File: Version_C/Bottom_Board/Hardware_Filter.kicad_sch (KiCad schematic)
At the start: 37 parts, among them U1 LM324, U2 LM324

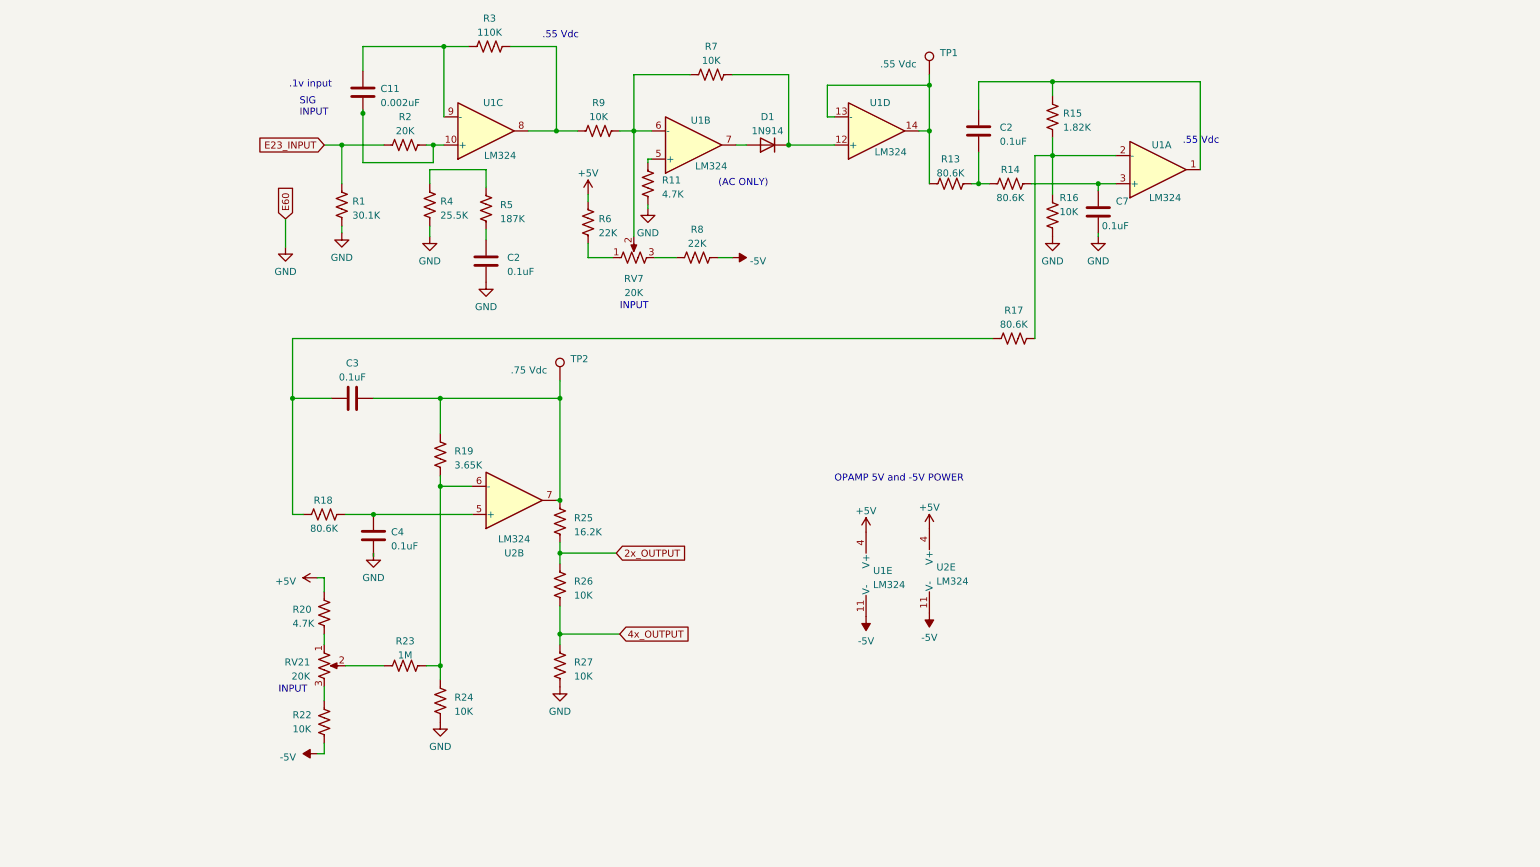
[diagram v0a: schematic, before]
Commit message: fixed directory overwrite
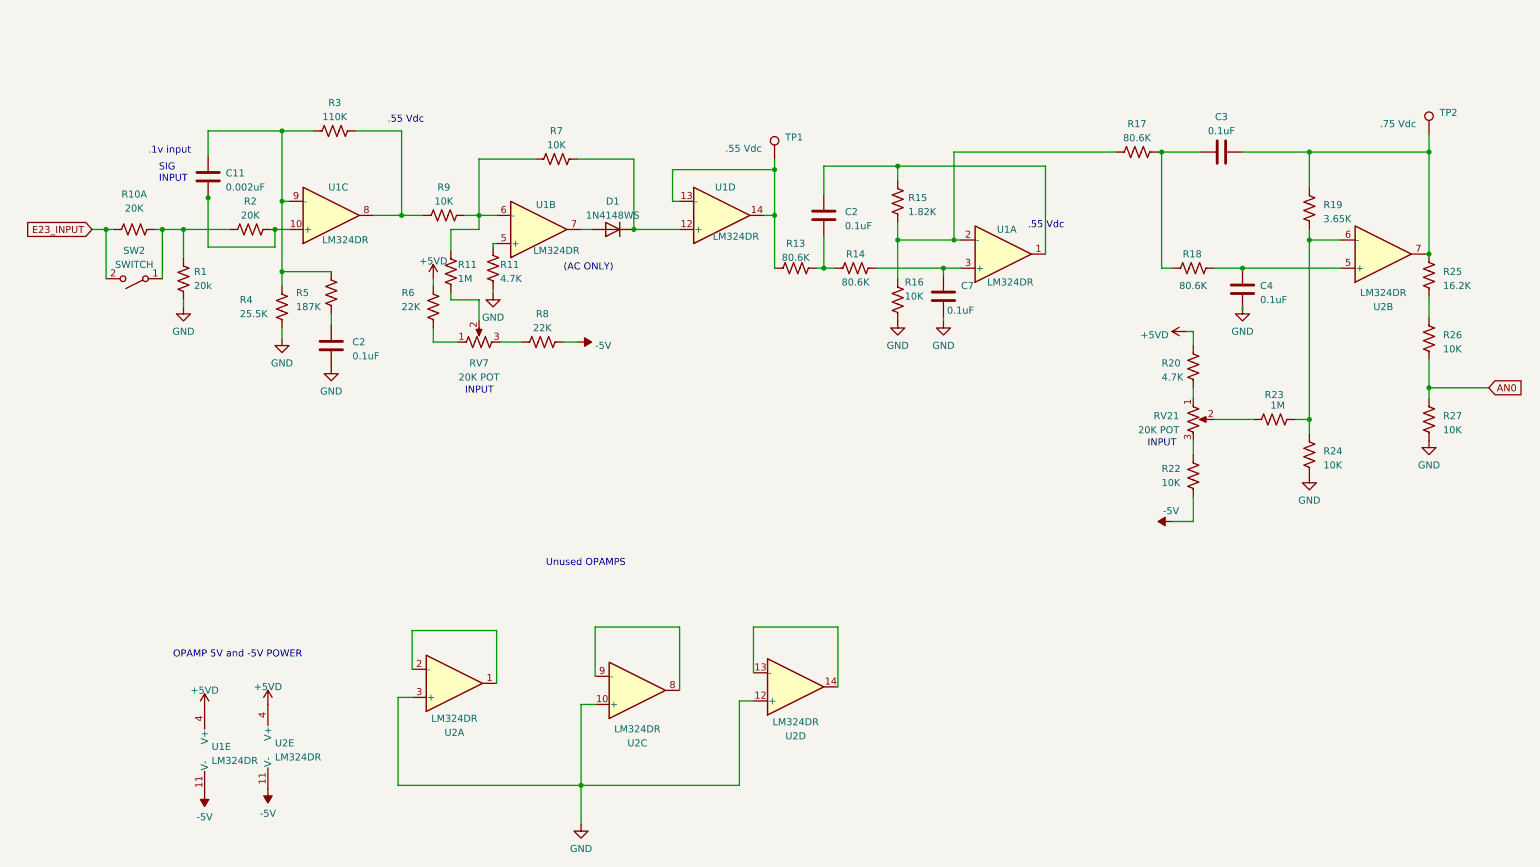
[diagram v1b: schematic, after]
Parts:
- added R10A: 20K, Resistor_SMD:R_0603_1608Metric, symbol Device:R_US
- added R11: 1M, Resistor_SMD:R_0603_1608Metric, symbol Device:R_US
- added SW2: SWITCH, symbol Switch:SW_SPST
- added unit 1 of U2
- added unit 4 of U2
- added unit 3 of U2
- D1: value 1N914 -> 1N4148WS; footprint Diode_SMD:D_0603_1608Metric -> bot_lib:Diode_1N4148WS
- R1: value 30.1K -> 20k
- RV21, RV7: value 20K -> 20K POT; footprint Potentiometer_THT:Potentiometer_Bourns_3386P_Vertical -> bot_lib:Potentiometer_Bourns_3386P_Vertical
- U1, U2: value LM324 -> LM324DR
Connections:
- net E23_INPUT: now also R10A.1, SW2.2 (B); no longer R1.1, R2.1
- net GND: now also U2.10 (+), U2.12 (+), U2.3 (+)
- net at R7.1, R9.2, U1.6 (-): now also R11.1; no longer RV7.2
- net at C11.1, R3.1, U1.9 (-): now also R4.1, R5.1
- net +5V renamed +5VD
- net 2x_OUTPUT: no longer names the net of R25.1, R26.2
- net 4x_OUTPUT renamed AN0
- new net: R11.2, RV7.2
- new net: R1.1, R10A.2, R2.1, SW2.1 (A)
- new net: U2.1, U2.2 (-)
- new net: U2.13 (-), U2.14
- new net: U2.8, U2.9 (-)
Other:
- note added: "Unused OPAMPS"
- company: (none) -> Secured Solutions Group
- title: (none) -> Current Monitoring System (Bottom Board)
- moved on the sheet: C11, C2, C3, C4, C7, D1, R1, R11, R13, R14, R15, R16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
